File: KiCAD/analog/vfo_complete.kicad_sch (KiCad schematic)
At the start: 22 parts, among them Q2 40673, Q3 2N3904, Q8 2N3904, U5 Si5351A_Breakout, U9 MCP4921

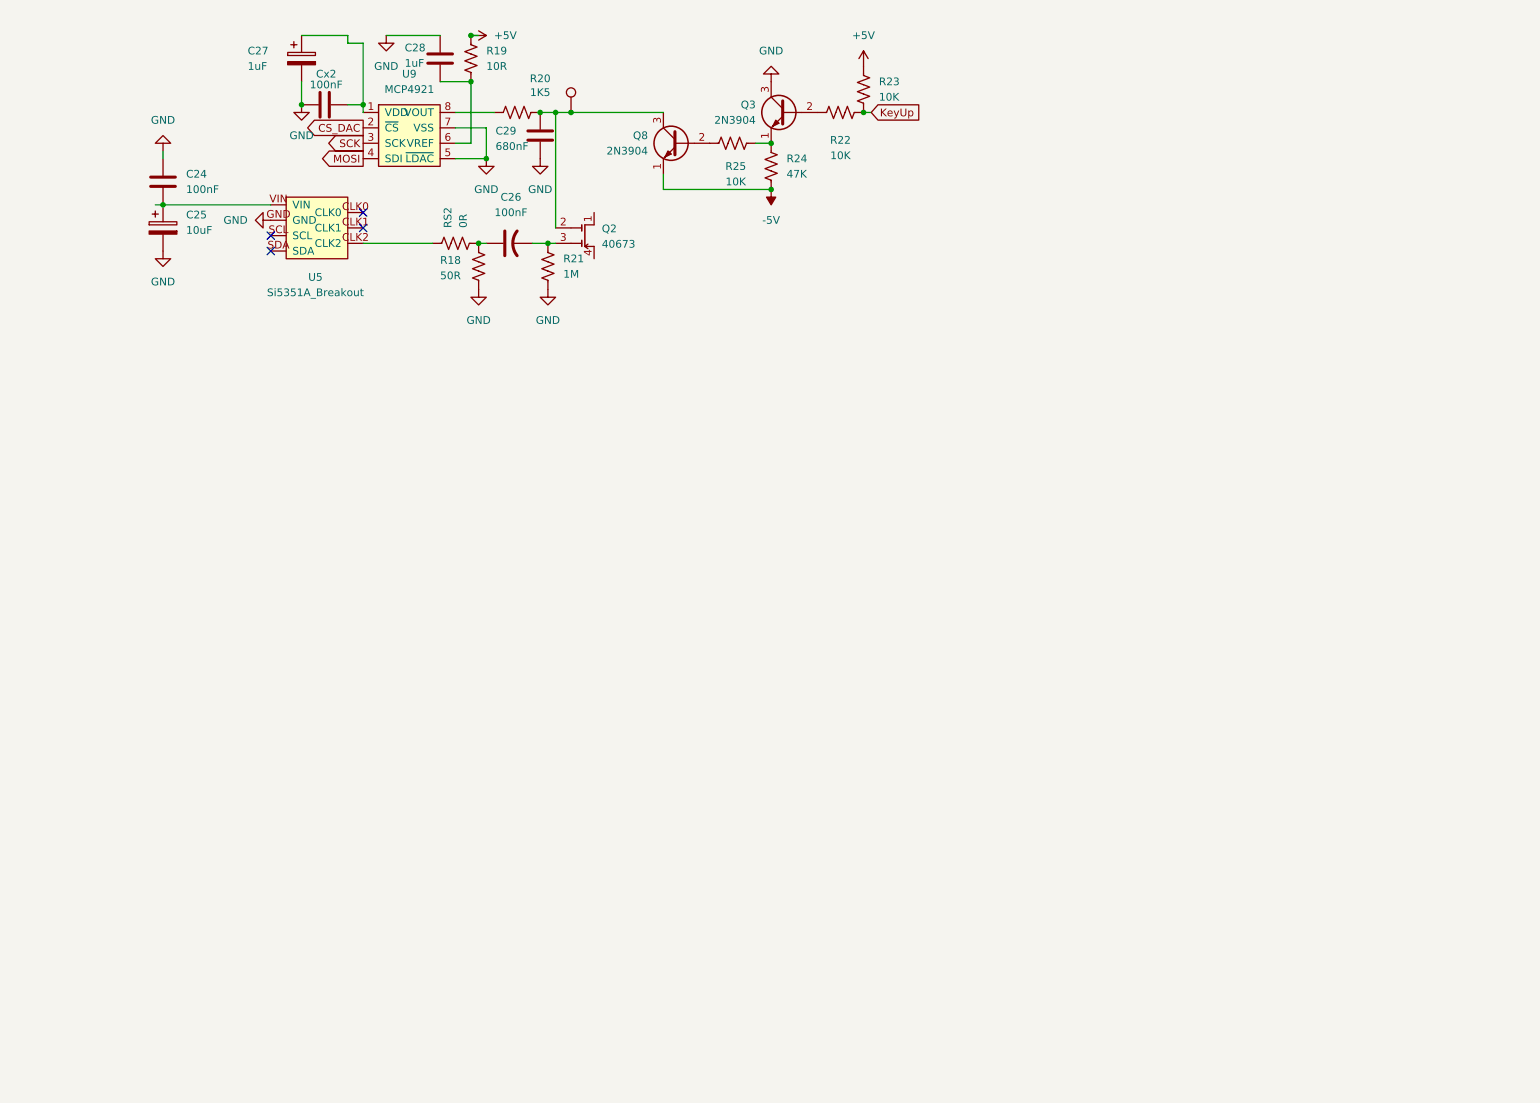
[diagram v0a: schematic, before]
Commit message: VFO_Complete: build out LM7171 op-amp chain + KeyUp gate rewire
Populates the three LM7171 stages driving the 12HG7 push-pull grids
via a phase-splitter topology, and reworks the KeyUp fail-safe.

- U10 (A0) front-end non-inverting, gain 5.7 (R32=1K, R33=4.7K)
- U11 (A2) non-inverting phase splitter, gain +4.25 (R34=1.2K, R35=3.9K)
- U12 (A1) inverting phase splitter, gain -4.25 (R37=5.1K, R38=1.2K)
- Cf phase-margin caps C69/C70 = 2 pF on the two splitter stages
- R36 = 0R jumper on U10-out -> U11-in wire (isolation-R placeholder)
- Q3 reworked from reversed-bias to proper emitter follower:
  collector to +5V, R24 (47K) as emitter load to GND
- -5V rail dropped from this sheet (was a single orphan pin)

Design captured in new Documentation/vfo_output_amp.md, including the
gain-matching trick (same Ri both splitter stages -> Rf1 = Rf2 + Ri
falls out algebraically) and HF precautions for LM7171 at 14 MHz.

Co-Authored-By: Claude Opus 4.7 <noreply@anthropic.com>
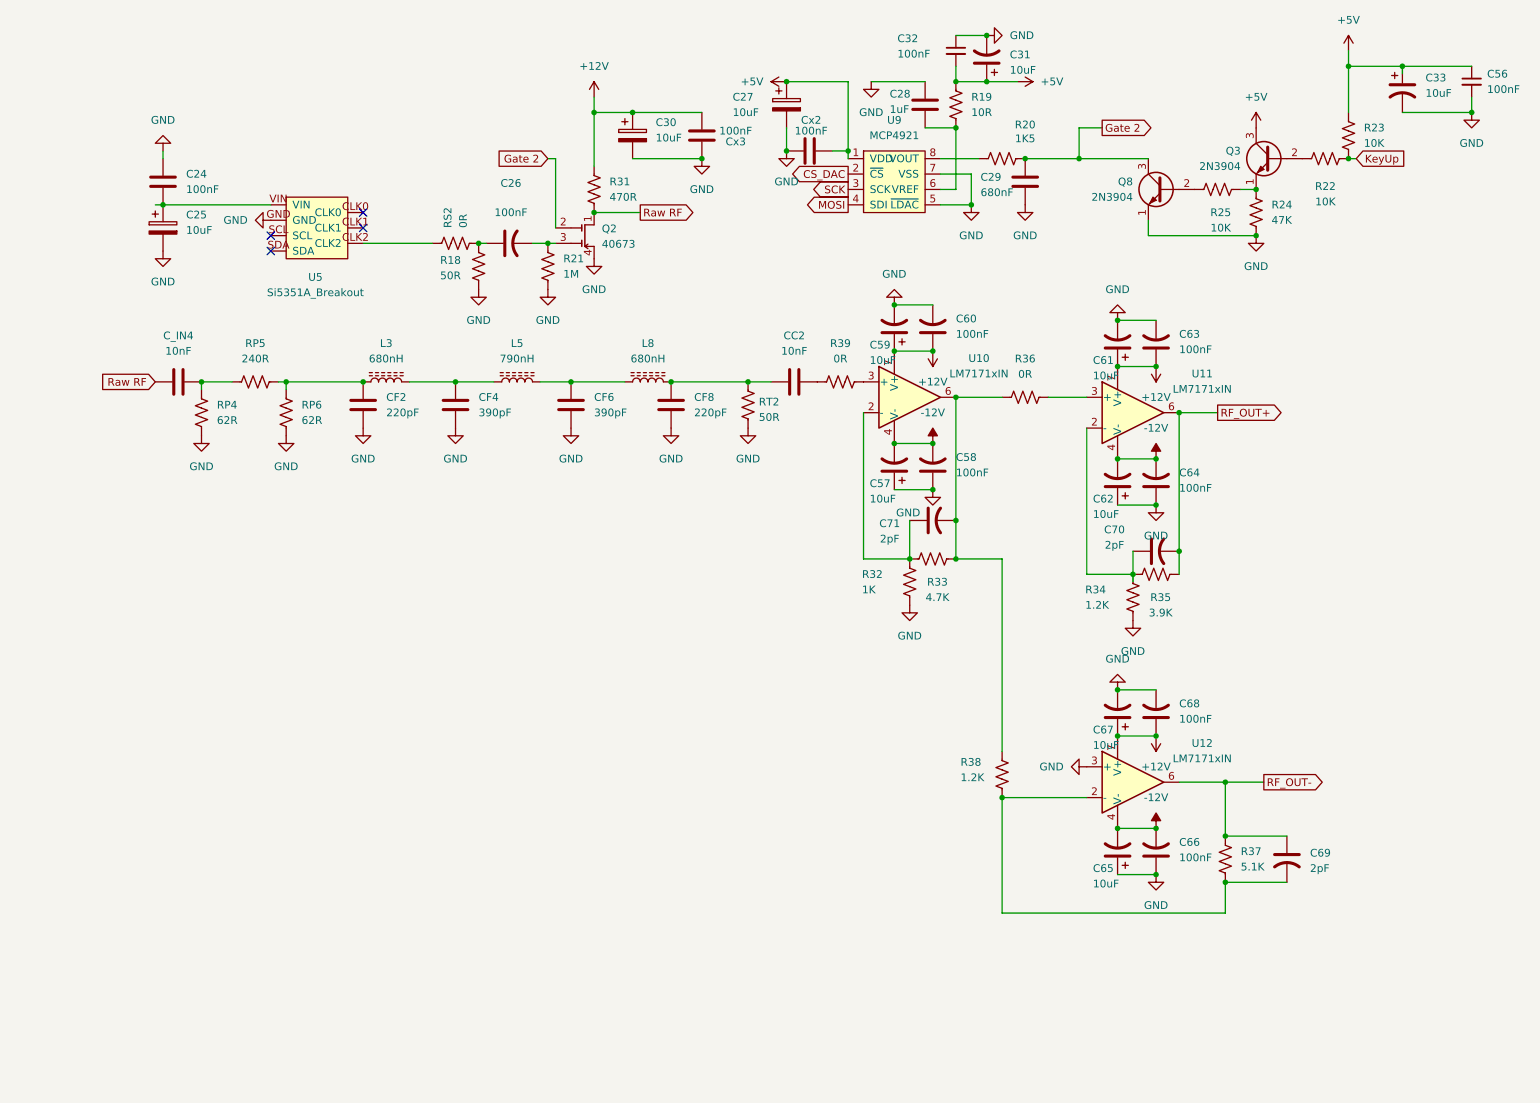
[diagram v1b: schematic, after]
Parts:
- removed TP24: Key_Out, Connector_PinHeader_2.54mm:PinHeader_1x01_P2.54mm_Vertical, symbol xmitter:xTP
- added C30: 10uF, symbol Device:C_Polarized
- added C31, C33, C57, C59, C61, C62, C65, C67: 10uF, symbol Device:C_Polarized_US
- added C32, C56: 100nF, symbol Device:C_Small
- added C58, C60, C63, C64, C66, C68: 100nF, symbol Device:C_US
- added C69, C70, C71: 2pF, symbol Device:C_US
- added CC2, C_IN4: 10nF, Capacitor_THT:C_Disc_D5.0mm_W2.5mm_P5.00mm, symbol Device:C
- added CF2, CF8: 220pF, Capacitor_THT:C_Disc_D6.0mm_W2.5mm_P5.00mm, symbol Device:C
- added CF4, CF6: 390pF, Capacitor_THT:C_Disc_D7.5mm_W2.5mm_P5.00mm, symbol Device:C
- added Cx3: 100nF, Capacitor_THT:C_Disc_D5.0mm_W2.5mm_P5.00mm, symbol Device:C
- added L3, L8: 680nH, xmitter:T68-6_Flat_HandWound, symbol Device:L_Ferrite
- added L5: 790nH, xmitter:T68-6_Vertical_HandWound, symbol Device:L_Ferrite
- added R31: 470R, symbol Device:R_US
- added R32: 1K, symbol Device:R_US
- added R33: 4.7K, symbol Device:R_US
- added R34, R38: 1.2K, symbol Device:R_US
- added R35: 3.9K, symbol Device:R_US
- added R36, R39: 0R, symbol Device:R_US
- added R37: 5.1K, symbol Device:R_US
- added RP4, RP6: 62R, Resistor_THT:R_Axial_DIN0207_L6.3mm_D2.5mm_P10.16mm_Horizontal, symbol Device:R_US
- added RP5: 240R, Resistor_THT:R_Axial_DIN0207_L6.3mm_D2.5mm_P10.16mm_Horizontal, symbol Device:R_US
- added RT2: 50R, Resistor_THT:R_Axial_DIN0207_L6.3mm_D2.5mm_P10.16mm_Horizontal, symbol Device:R_US
- added U10, U11, U12: LM7171xIN, Package_DIP:DIP-8_W7.62mm, symbol Amplifier_Operational:LM7171xIN
- C27: value 1uF -> 10uF
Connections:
- net -5V is gone; now on net GND: Q8.1 (E), R24.2
- net +5V: now also C27.1, Cx2.2, Q3.3 (C), U9.1 (VDD), C31.1, C32.2, C33.1, C56.1
- net GND: now also Q2.4 (S), C30.2, C31.2, C32.1, C33.2, C56.2, C57.1, C58.1, C59.2, C60.2, C61.2, C62.1, C63.2, C64.1, C65.1, C66.1, C67.2, C68.2, CF2.2, CF4.2, CF6.2, CF8.2, Cx3.1, R32.2, R34.2, RP4.2, RP6.2, RT2.2, U12.3 (+); no longer Q3.3 (C)
- net Gate 2: now reaches C29.1, Q2.2 (G2), Q8.3 (C), R20.2
- net Raw RF: now reaches Q2.1 (D)
- net Raw RF: now also C_IN4.1, R31.2
- new net: C_IN4.2, RP4.1, RP5.1
- new net: C70.1, R34.1, R35.1, U11.2 (-)
- new net: CC2.1, CF8.1, L8.2, RT2.1
- new net: C71.1, R32.1, R33.1, U10.2 (-)
- new net: C71.2, R33.2, R36.1, R38.1, U10.6
- new net: C69.2, R37.1, R38.2, U12.2 (-)
- new net: CF6.1, L5.2, L8.1
- new net: R36.2, U11.3 (+)
- new net: CC2.2, R39.1
- new net: R39.2, U10.3 (+)
- new net: CF2.1, L3.1, RP5.2, RP6.1
- new net: CF4.1, L3.2, L5.1
- new net +12V: C30.1, C59.1, C60.1, C61.1, C63.1, C67.1, C68.1, Cx3.2, R31.1, U10.7 (V+), U11.7 (V+), U12.7 (V+)
- new net -12V: C57.2, C58.2, C62.2, C64.2, C65.2, C66.2, U10.4 (V-), U11.4 (V-), U12.4 (V-)
- new net RF_OUT+: C70.2, R35.2, U11.6
- new net RF_OUT-: C69.1, R37.2, U12.6
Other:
- moved on the sheet: C27, C28, C29, Cx2, Q3, Q8, R19, R20, R22, R23, R24, R25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

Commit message: KiCad revB: remove obsolete VFO sheets, add J3 footprint, add datasheets
- analog.kicad_sch: dropped VFO and VFO_Buffer_keyer sheets (legacy
  stubs superseded by VFO_Complete). Underlying vfo.kicad_sch and
  buffer_keyer.kicad_sch files deleted. PCB and .kicad_pro refreshed
  to match after Update PCB from Schematic.
- vfo_complete.kicad_sch: J3 (AC input to the +/-12V bridge) gets
  Phoenix Contact MKDS 1,5/2 footprint and a link to the local
  datasheet copy.
- Documentation/Components/: local datasheet copies for parts in the
  current supply bring-up (LM317L, LT1054, LM7800 series, 1N5817,
  2N3904/6, Kemet MLCC leaded, Phoenix Contact 142RHS).
- Documentation/Capacitors_Ordered.xlsx: capacitor inventory summary
  compiled from the Mouser and Digi-Key invoices, for stock-consistent
  reordering.

Co-Authored-By: Claude Opus 4.7 <noreply@anthropic.com>
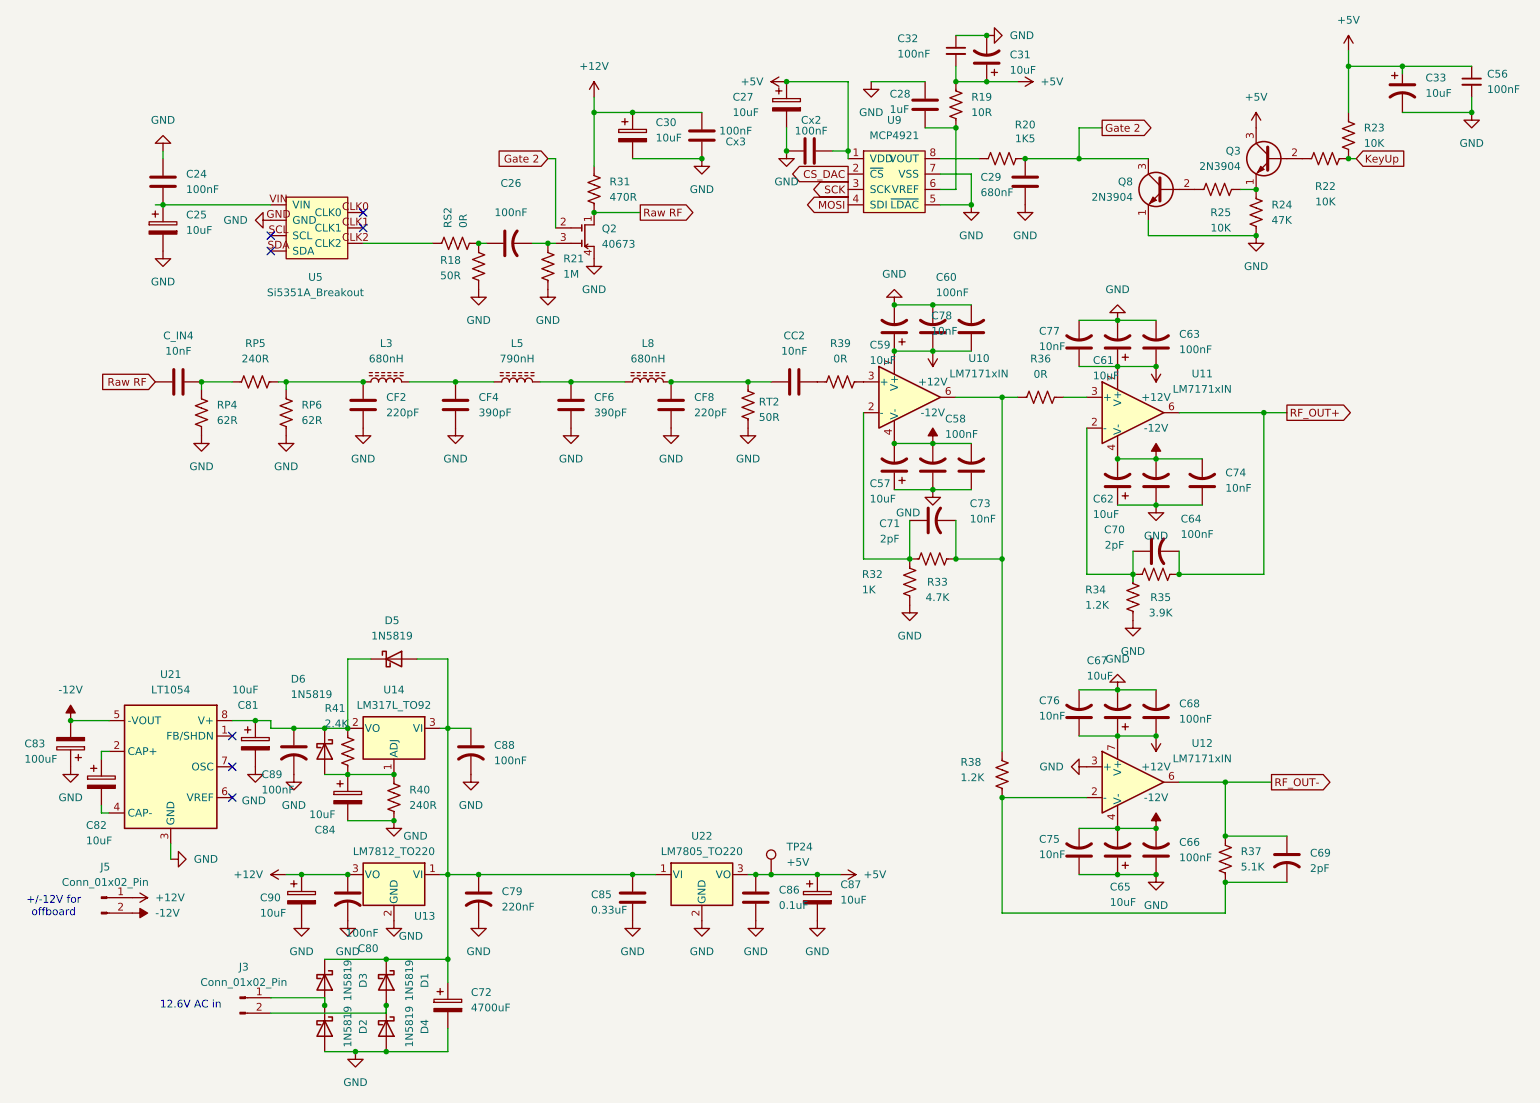
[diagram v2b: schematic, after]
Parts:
- added C72: 4700uF, symbol Device:C_Polarized
- added C73, C74, C75, C76, C77, C78: 10nF, symbol Device:C_US
- added C79: 220nF, symbol Device:C_US
- added C80, C88, C89: 100nF, symbol Device:C_US
- added C81, C82, C84, C90: 10uF, symbol Device:C_Polarized
- added C83: 100uF, symbol Device:C_Polarized
- added C85: 0.33uF, Capacitor_THT:C_Rect_L7.0mm_W3.5mm_P5.00mm, symbol Device:C
- added C86: 0.1uF, Capacitor_THT:C_Disc_D5.0mm_W2.5mm_P5.00mm, symbol Device:C
- added C87: 10uF, Capacitor_THT:CP_Radial_D5.0mm_P2.00mm, symbol Device:C_Polarized
- added D1, D2, D3, D4, D5, D6: 1N5819, Diode_THT:D_DO-41_SOD81_P10.16mm_Horizontal, symbol Diode:1N5819
- added J3, J5: Conn_01x02_Pin, TerminalBlock_Phoenix:TerminalBlock_Phoenix_MKDS-1,5-2_1x02_P5.00mm_Horizontal, symbol Connector:Conn_01x02_Pin
- added R40: 240R, symbol Device:R_US
- added R41: 2.4K, symbol Device:R_US
- added TP24: +5V, Connector_PinHeader_2.54mm:PinHeader_1x01_P2.54mm_Vertical, symbol xmitter:xTP
- added U13: LM7812_TO220, Package_TO_SOT_THT:TO-220-3_Vertical, symbol Regulator_Linear:LM7812_TO220
- added U14: LM317L_TO92, Package_TO_SOT_THT:TO-92_Inline, symbol Regulator_Linear:LM317L_TO92
- added U21: LT1054, symbol Regulator_SwitchedCapacitor:LT1054
- added U22: LM7805_TO220, Package_TO_SOT_THT:TO-220-3_Vertical, symbol Regulator_Linear:LM7805_TO220
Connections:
- net +12V: now also C76.1, C77.1, C78.1, C80.1, C90.1, J5.1 (Pin_1), U13.3 (VO)
- net +5V: now also C86.1, C87.1, TP24.1, U22.3 (VO)
- net -12V: now also C73.2, C74.2, C75.2, C83.2, J5.2 (Pin_2), U21.5 (-VOUT)
- net GND: now also C72.2, C73.1, C74.1, C75.1, C76.2, C77.2, C78.2, C79.2, C80.2, C81.2, C83.1, C84.2, C85.2, C86.2, C87.2, C88.2, C89.2, C90.2, D2.2 (A), D4.2 (A), R40.2, U13.2 (GND), U21.3 (GND), U22.2 (GND)
- new net: C72.1, C79.1, C85.1, C88.1, D1.1 (K), D3.1 (K), D5.2 (A), U13.1 (VI), U14.3 (VI), U22.1 (VI)
- new net: D1.2 (A), D4.1 (K), J3.2 (Pin_2)
- new net: D2.1 (K), D3.2 (A), J3.1 (Pin_1)
- new net: C81.1, C89.1, D5.1 (K), D6.1 (K), R41.1, U14.2 (VO), U21.8 (V+)
- new net: C84.1, D6.2 (A), R40.1, R41.2, U14.1 (ADJ)
- new net: C82.1, U21.2 (CAP+)
- new net: C82.2, U21.4 (CAP-)
- no-connect marks 4 -> 7
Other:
- note added: "+/-12V for offboard"
- note added: "12.6V AC in"
- moved on the sheet: R36

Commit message: KiCad revB: analog board schematic edits + op-amp balance analysis doc
- vfo_complete.kicad_sch and arduino.kicad_sch: accumulated schematic
  edits (op-amp area, C1/C2 DC-block confirmed on push-pull outputs,
  general cleanup).
- Documentation/op_amp_pushpull_balance.md: closed-form analysis of
  U11/U12 push-pull balance at 14 MHz with four balancing options
  (leave alone, match Rf, match Rin, adjust comp caps) and CMRR /
  amplitude / phase results for each.

Co-Authored-By: Claude Opus 4.7 <noreply@anthropic.com>
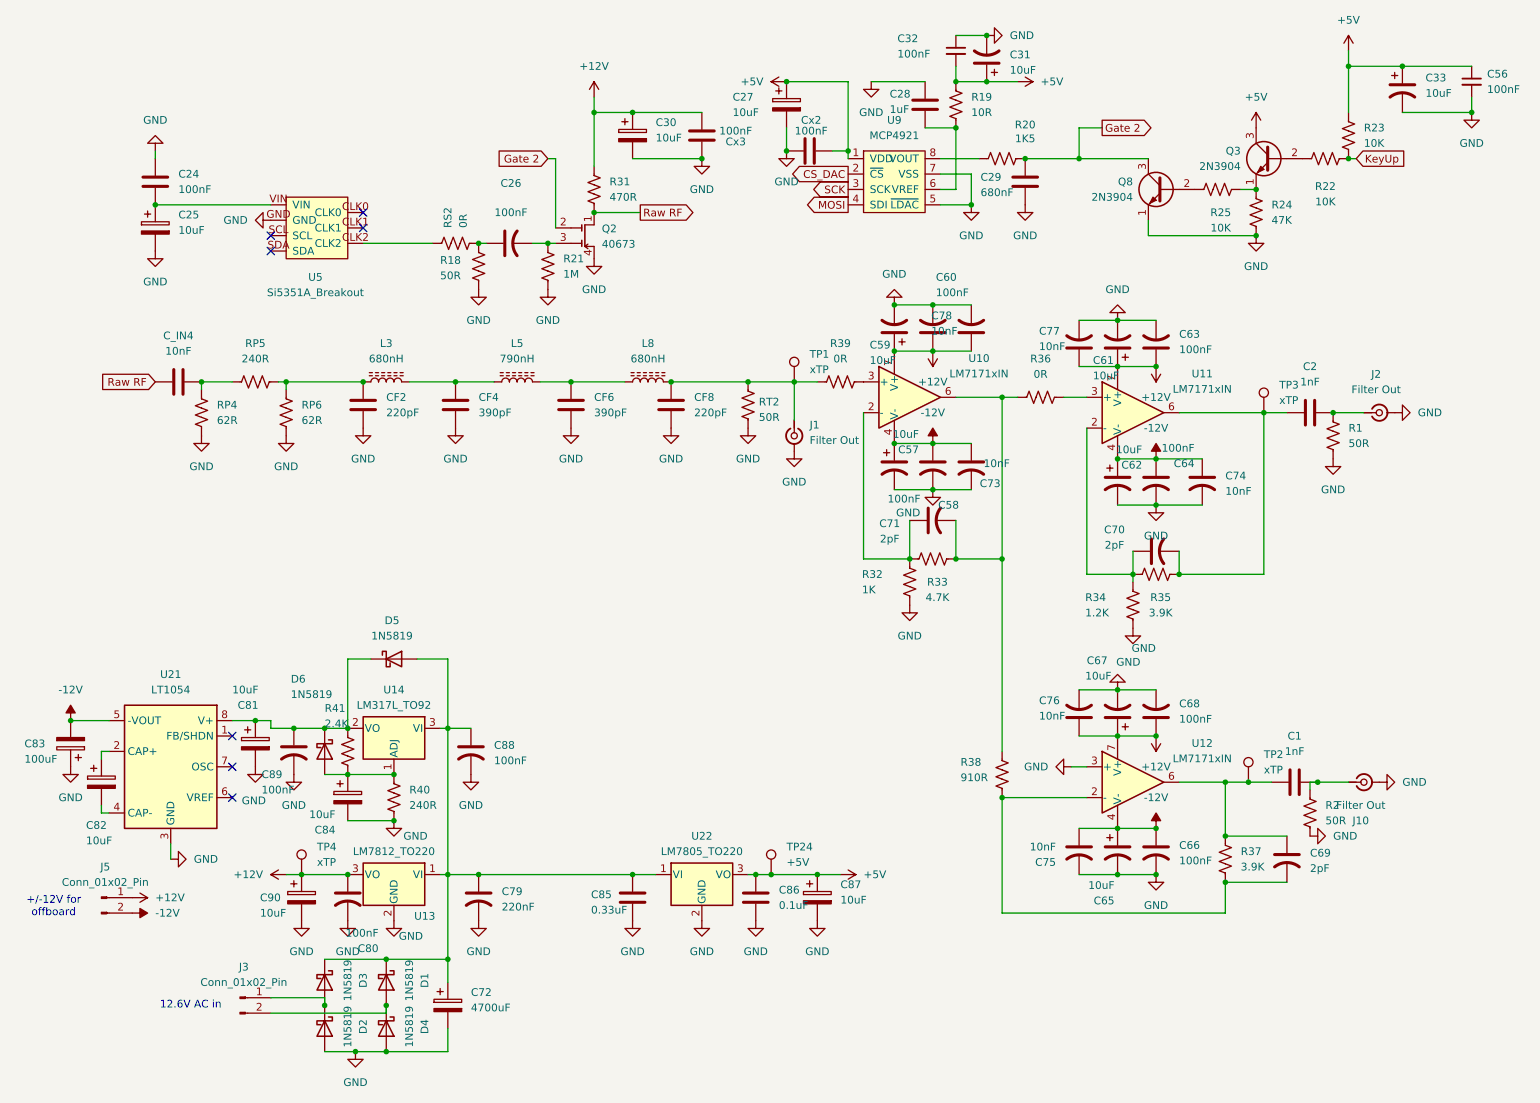
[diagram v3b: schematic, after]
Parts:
- removed CC2: 10nF, Capacitor_THT:C_Disc_D5.0mm_W2.5mm_P5.00mm, symbol Device:C
- added C1, C2: 1nF, symbol Device:C
- added J1, J10, J2: Filter Out, Connector_Coaxial:SMA_Amphenol_132134_Vertical, symbol Connector:Conn_Coaxial_Small
- added R1, R2: 50R, symbol Device:R_US
- added TP1, TP2, TP3, TP4: xTP, Connector_PinHeader_2.54mm:PinHeader_1x01_P2.54mm_Vertical, symbol xmitter:xTP
- R37: value 5.1K -> 3.9K
- R38: value 1.2K -> 910R
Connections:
- net +12V: now also TP4.1
- net -12V: now also C57.1, C58.1, C62.1, C64.1, C65.1, C66.1, C73.1, C74.1, C75.1; no longer C57.2, C58.2, C62.2, C64.2, C65.2, C66.2, C73.2, C74.2, C75.2
- net GND: now also C57.2, C58.2, C62.2, C64.2, C65.2, C66.2, C73.2, C74.2, C75.2, J1.2 (Ext), J10.2 (Ext), J2.2 (Ext), R1.2, R2.2; no longer C57.1, C58.1, C62.1, C64.1, C65.1, C66.1, C73.1, C74.1, C75.1
- net at CF8.1, L8.2, RT2.1: now also R39.1, J1.1 (In), TP1.1
- net RF_OUT+: no longer names the net of C70.2, R35.2, U11.6
- net RF_OUT+: now also C2.1, TP3.1
- net RF_OUT-: no longer names the net of C69.1, R37.2, U12.6
- net RF_OUT-: now also C1.1, TP2.1
- new net: C1.2, J10.1 (In), R2.1
- new net: C2.2, J2.1 (In), R1.1
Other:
- moved on the sheet: C24, C25
